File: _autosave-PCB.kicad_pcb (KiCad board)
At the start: 2 copper layers, 60 x 60 mm, 50 parts, among them J1 USB_C_Receptacle_USB2.0_16P, J2 Conn_01x04_Pin, J3 Conn_01x04_Pin, J4 Conn_01x04_Pin, J5 Conn_01x02_Pin, J6 Conn_01x02_Pin, J7 Conn_01x02_Pin, SW1 SW_Push, SW2 SW_Push, U1 TMC2209_SILENTSTEPSTICK, U2 TMC2209_SILENTSTEPSTICK, U3 D3V3XA4B10LP, U4 AMS1117-3.3 (UMW), U5 TMC2209_SILENTSTEPSTICK, U6 ESP32-S3-WROOM-1

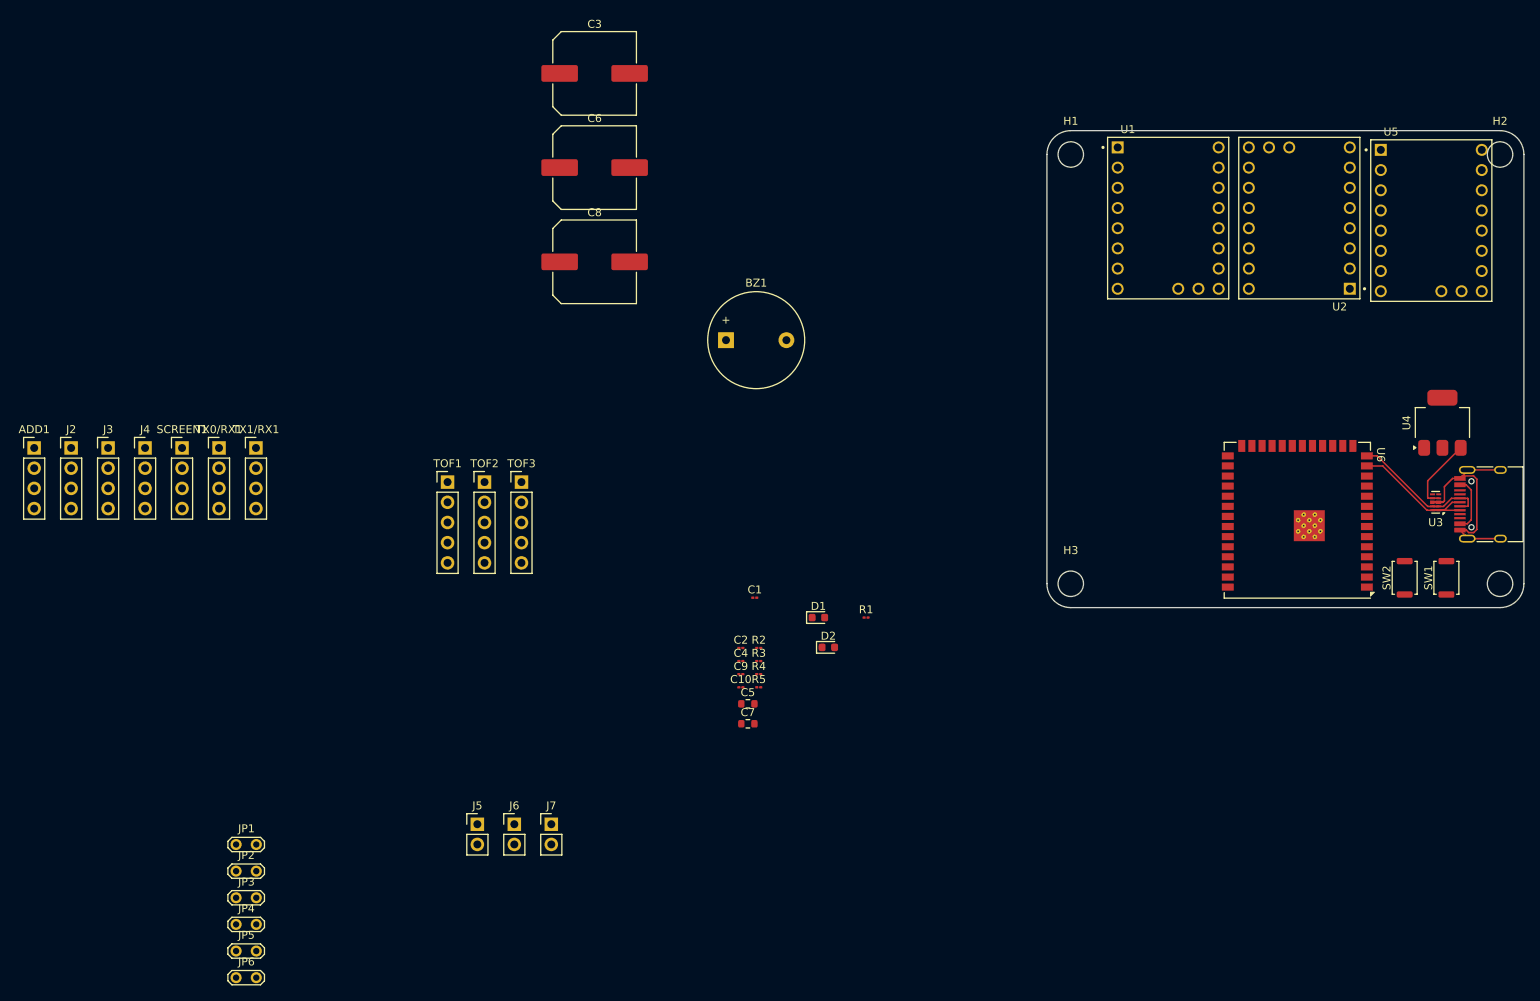
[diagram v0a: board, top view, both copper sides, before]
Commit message: Fix court-circuit
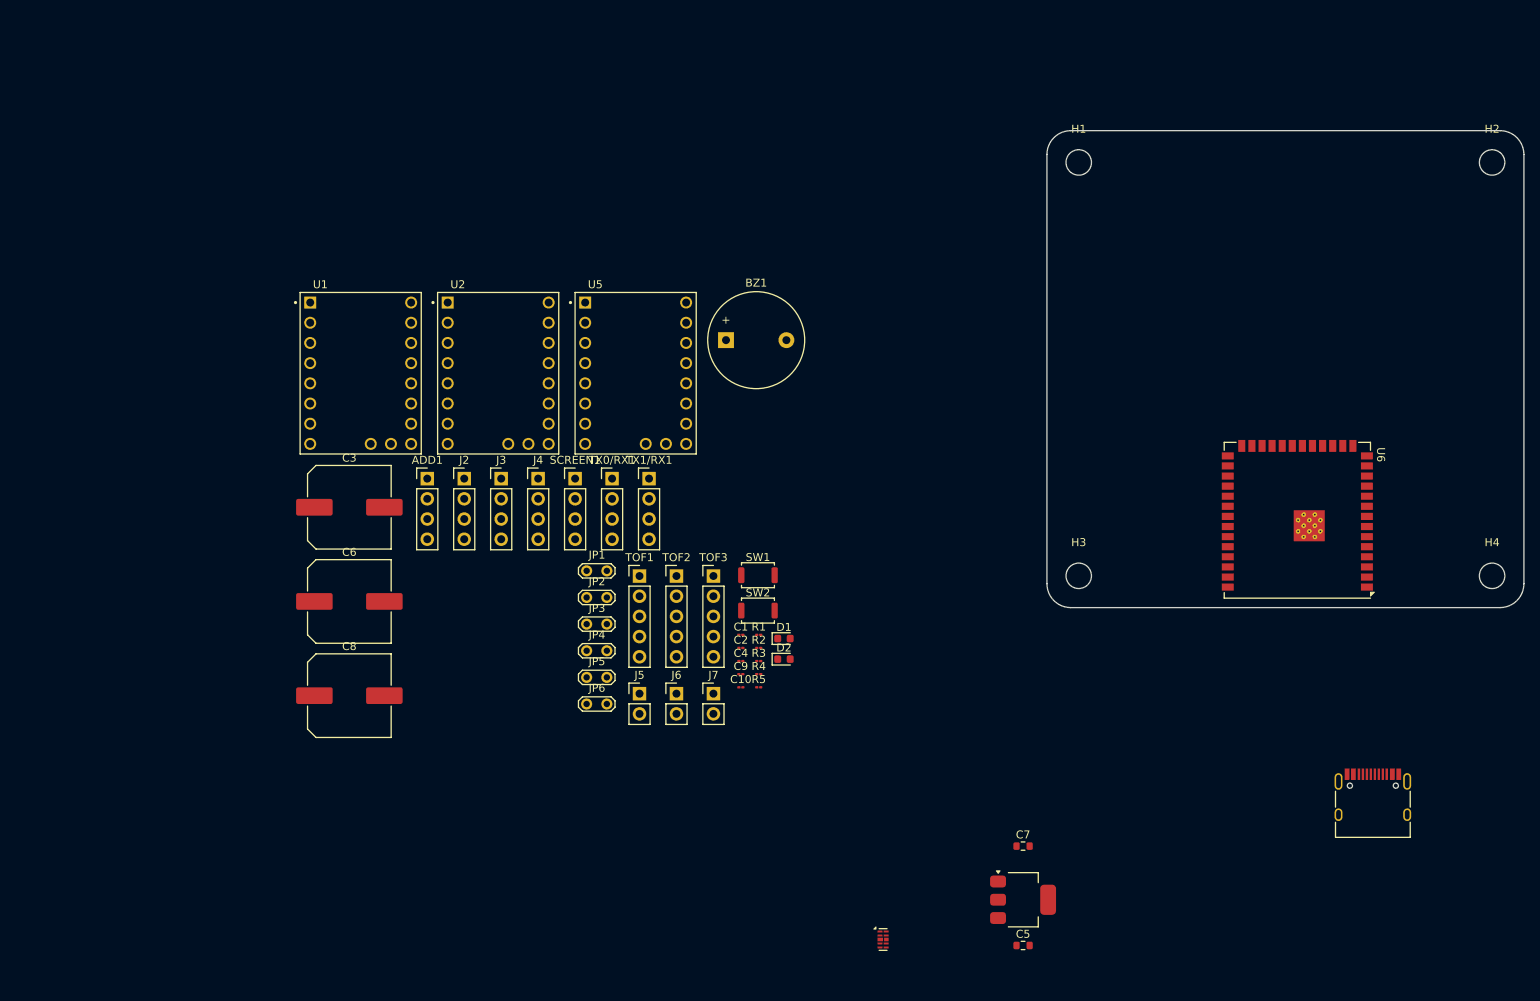
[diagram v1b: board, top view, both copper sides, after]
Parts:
- moved U1 103.4 mm to (123.7, 77.5)
- moved U2 102.7 mm to (141.0, 77.5), turned to 0 degrees
- moved U5 101.9 mm to (158.3, 77.5)
- moved U3 88.6 mm to (189.4, 148.8), turned to 0 degrees
- moved SW1 86.6 mm to (173.6, 102.9), turned to 0 degrees
- moved SW2 81.5 mm to (173.6, 107.4), turned to 0 degrees
- moved U4 79.9 mm to (207.0, 143.8), turned to 0 degrees
- moved C3 62.7 mm to (122.2, 94.4)
- moved C8 62.7 mm to (122.2, 118.1)
- moved C6 62.7 mm to (122.2, 106.2)
- moved JP1 55.9 mm to (152.1, 102.4)
- moved JP2 55.9 mm to (152.1, 105.7)
- moved JP6 55.9 mm to (152.1, 119.1)
- moved JP3 55.9 mm to (152.1, 109.1)
- moved JP4 55.9 mm to (152.1, 112.4)
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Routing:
- net 3V3: track 29.5 -> 0.00 mm
- net USB_N: track 18.6 -> 0.00 mm
- net USB_P: track 18.5 -> 0.00 mm
- net VCC_5V: track 9.40 -> 0.00 mm
- net VCC_5Vin: track 7.08 -> 0.00 mm
